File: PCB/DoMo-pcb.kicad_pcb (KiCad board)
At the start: 2 copper layers, 84.9 x 65.1 mm, 31 parts, among them SW0 SW_Push, SW1 Rotary_Encoder_Switch, SW10 SW_Push, SW2 SW_Push, SW3 SW_Push, SW4 SW_Push, SW5 SW_Push, SW6 SW_Push, SW7 SW_Push, SW8 SW_Push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

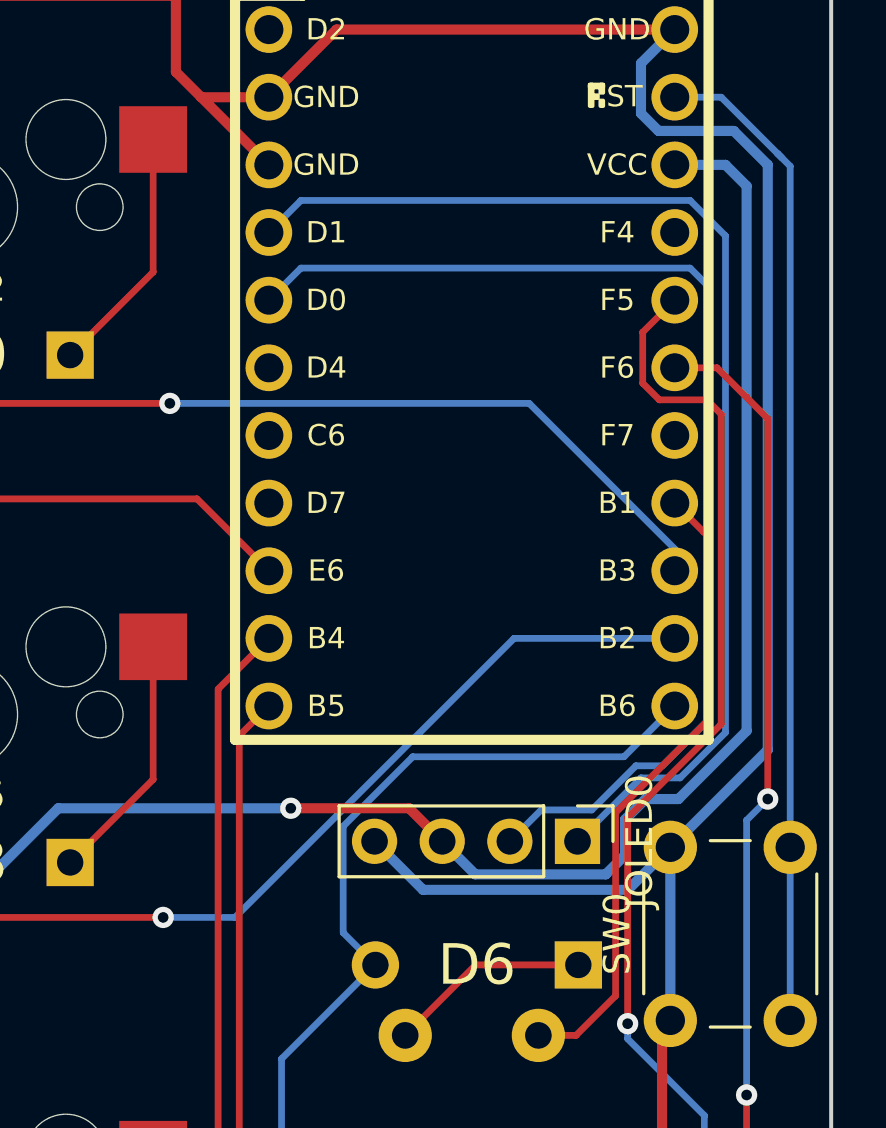
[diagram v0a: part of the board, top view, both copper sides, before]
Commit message: fix 1x4 connector
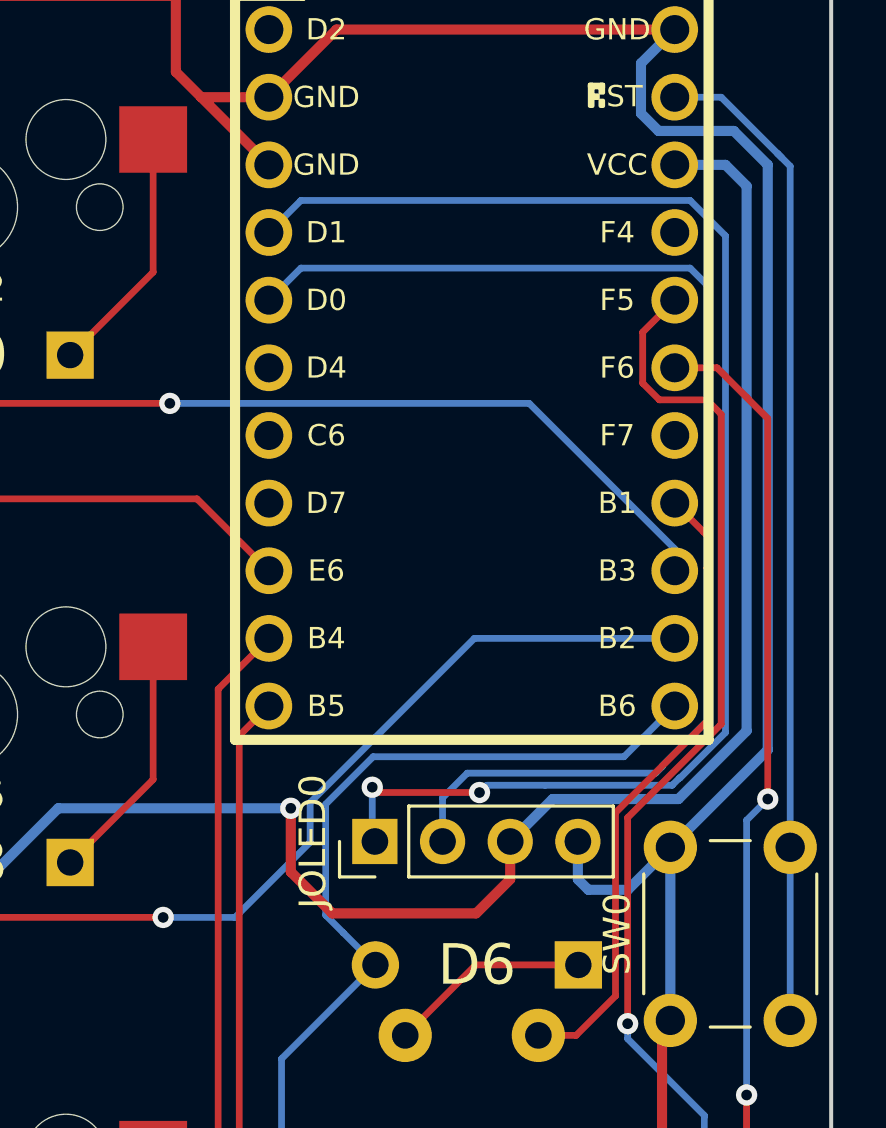
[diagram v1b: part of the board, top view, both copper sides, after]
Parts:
- moved JOLED0 7.61 mm to (239.2, 92.9), turned to 90 degrees
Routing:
- net SDA: track 44.1 -> 53.2 mm, vias 0 -> 2
- net GND: track 230.3 -> 223.5 mm
- net SCL: track 42.9 -> 46.4 mm
- net VCC: track 193.3 -> 196.0 mm
- net R2: track 98.8 -> 100.2 mm
- net R1: track 79.9 -> 80.8 mm
